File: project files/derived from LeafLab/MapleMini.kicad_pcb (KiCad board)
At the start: 2 copper layers, 50.8 x 17.8 mm, 39 parts, among them J1 USB_C, J2 Left, J3 Right, Q1 BC817, Q2 BC817, SW1 Reset, SW2 Button, U1 MCP1703A-3302_SOT23, U2 MCP1703A-3302_SOT23, U3 STM32F103CBTx, Y1 8MHz

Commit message: Diode search
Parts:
- D1: footprint Diode_SMD:D_SOD-323 -> Diode_SMD:D_SOD-123
- L1: value L -> 10uH
- moved D1 21.5 mm to (100.7, 100.3)
- moved J2 15.2 mm to (52.1, 77.5)
- moved J3 15.2 mm to (52.1, 92.7)
- moved D2 5.72 mm to (73.3, 85.1)
- moved U3 5.08 mm to (73.7, 85.1), turned to 315 degrees
- moved SW2 3.81 mm to (91.4, 85.1)
- moved SW1 1.70 mm to (96.5, 85.1)

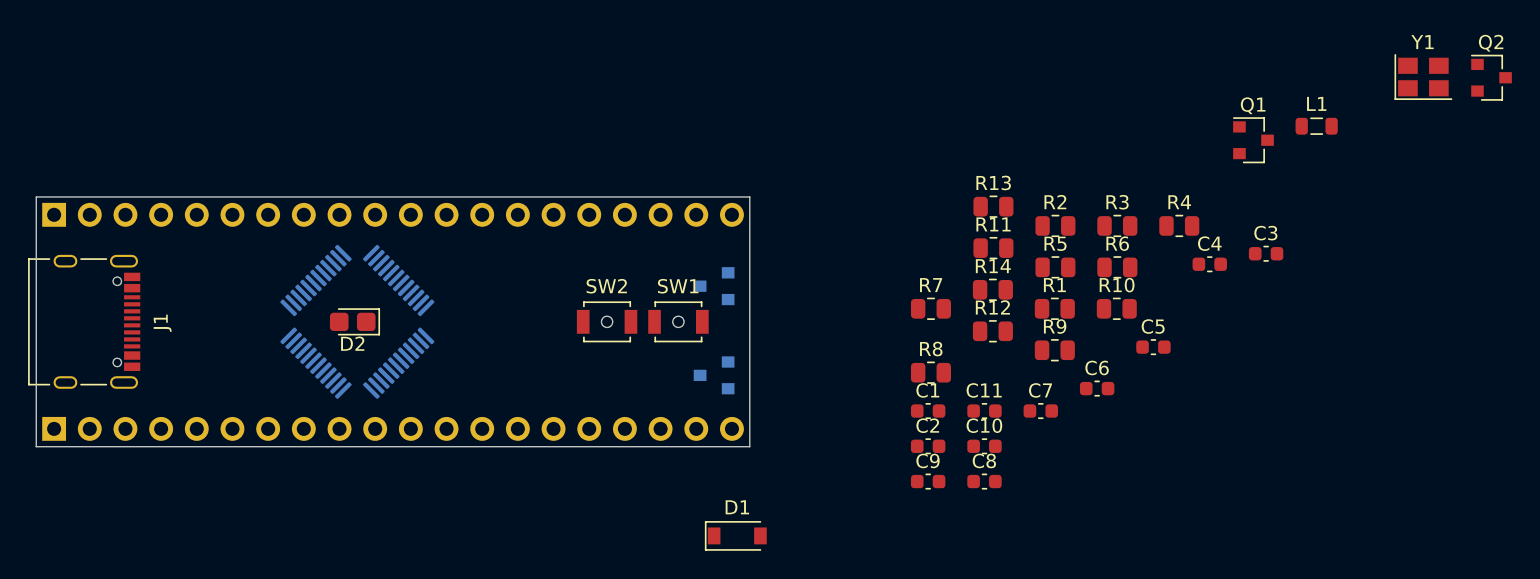
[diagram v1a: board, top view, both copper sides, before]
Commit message: Added STDC connectors
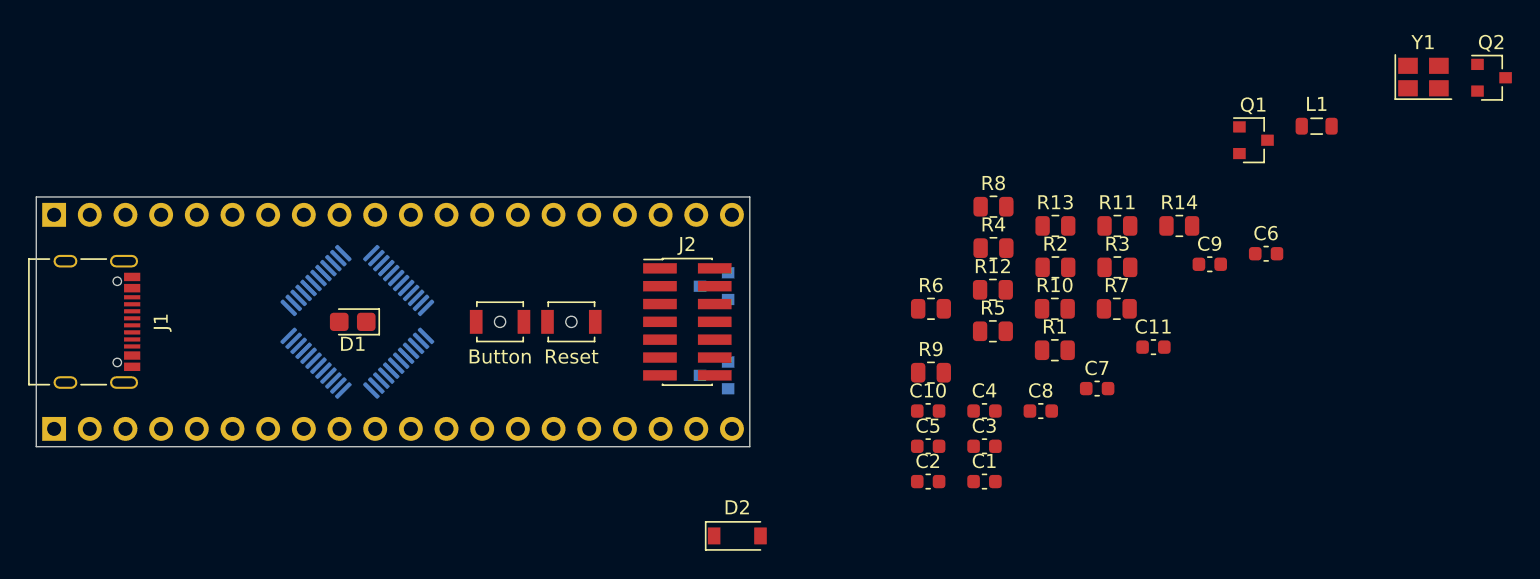
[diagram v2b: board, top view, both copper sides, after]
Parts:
- added J2: Conn_ST_STDC14, Connector_PinHeader_1.27mm:PinHeader_2x07_P1.27mm_Vertical_SMD, F.Cu at (97.2, 85.1)
- moved SW2 7.62 mm to (83.8, 85.1)
- moved SW1 7.62 mm to (88.9, 85.1)
- renumbered C8 to C1, C1 to C10, C5 to C11, C9 to C2, C10 to C3, C11 to C4, C2 to C5, C3 to C6, C6 to C7, C7 to C8, C4 to C9, D2 to D1, D1 to D2, J2 to J3, J3 to J4, R9 to R1, R1 to R10, R3 to R11, R14 to R12, R2 to R13, R4 to R14, R5 to R2, R6 to R3, R11 to R4, R12 to R5, R7 to R6, R10 to R7, R13 to R8, R8 to R9, U3 to U1, U1 to U2, U2 to U3
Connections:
- net /0 renamed SWDIO
- net /1 renamed SWCLK
- net /19 renamed SWO
- net /25 renamed RX
- net /26 renamed TX

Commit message: power nets renaming
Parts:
- D2, Q1, Q2, Y1: moved to B.Cu
- moved Q2 94.7 mm to (61.0, 83.2), turned to 180 degrees
- moved Y1 85.4 mm to (65.4, 81.9), turned to 180 degrees
- moved Q1 77.9 mm to (61.0, 87.0), turned to 180 degrees
- moved R1 62.6 mm to (60.7, 86.4), turned to 180 degrees
- moved C7 61.5 mm to (65.4, 81.3)
- moved C8 57.6 mm to (65.4, 82.5), turned to 180 degrees
- moved R6 53.3 mm to (61.2, 84.2), turned to 180 degrees
- moved D2 19.8 mm to (98.8, 80.6), turned to 180 degrees
- moved U2 2.86 mm to (99.1, 85.4)
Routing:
- net SWCLK: track 0.00 -> 8.47 mm
- net SWDIO: track 0.00 -> 8.01 mm
